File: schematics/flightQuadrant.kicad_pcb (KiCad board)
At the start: 2 copper layers, 50 x 62.5 mm, 15 parts, among them J1 Jack-DC, M1 M_ENG1, M2 M_ENG2, M3 M_BRK, M4 M_FLP, U1 L293D, U2 L293D

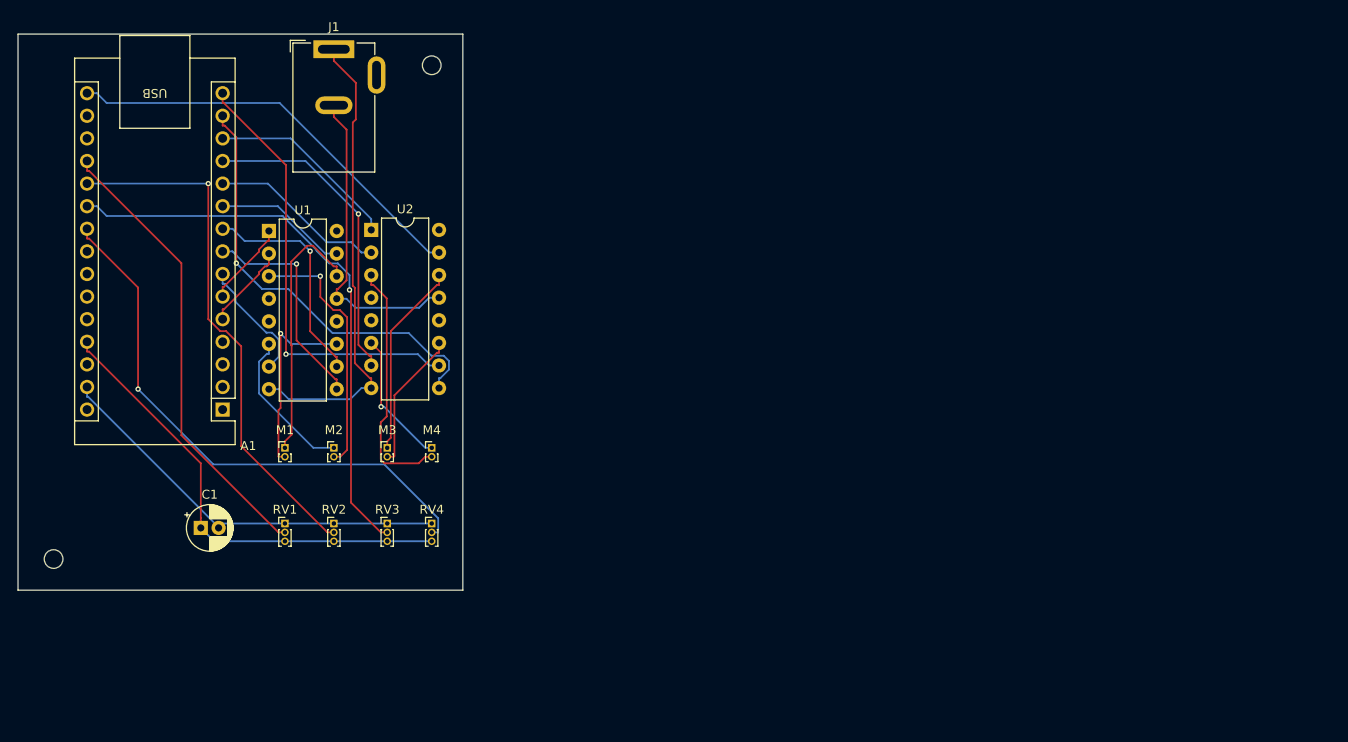
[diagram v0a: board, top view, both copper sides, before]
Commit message: Migrate to teeensyyyy 3.2
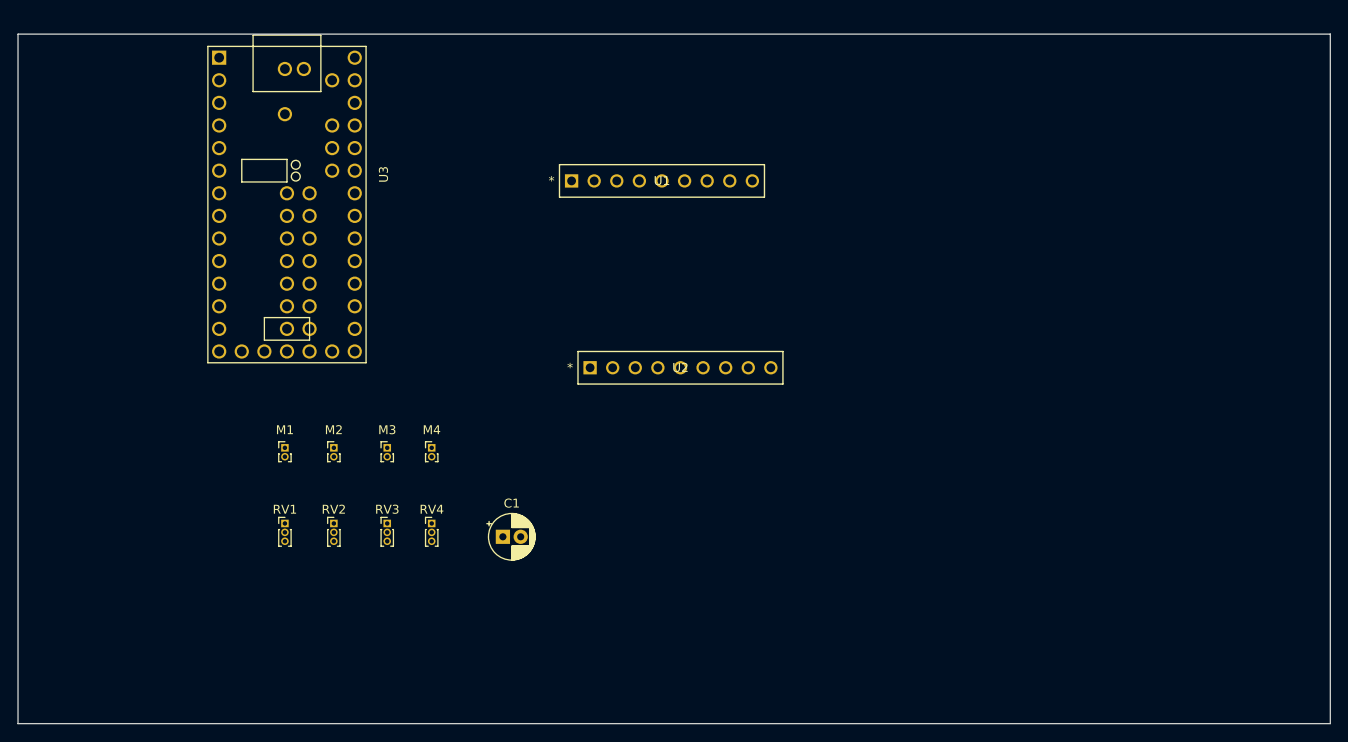
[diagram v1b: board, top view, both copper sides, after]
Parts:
- removed A1: Arduino_Nano_v3.x, Module:Arduino_Nano
- removed J1: Jack-DC, Connector_BarrelJack:BarrelJack_GCT_DCJ200-10-A_Horizontal
- removed REF**, p: MountingHole_2.1mm, MountingHole:MountingHole_2.1mm
- added U3: Teensy3.2, Teensy:Teensy30_31_32_All_Pins, F.Cu at (118.7, 63.2)
- U1, U2: value L293D -> ta7291sgo; footprint Package_DIP:DIP-16_W7.62mm -> TADriver:SIP9_TOS
- moved U1 34.5 mm to (150.7, 60.5)
- moved C1 34.0 mm to (143.0, 100.5)
- moved U2 29.1 mm to (152.8, 81.5)
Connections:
- M1 pad 1: Net-(U1-4Y) -> unconnected-(M1-Pad1)
- M1 pad 2: Net-(U1-3Y) -> unconnected-(M1-Pad2)
- M2 pad 1: Net-(U1-2Y) -> unconnected-(M2-Pad1)
- M2 pad 2: Net-(U1-1Y) -> unconnected-(M2-Pad2)
- M3 pad 1: Net-(U2-4Y) -> unconnected-(M3-Pad1)
- M3 pad 2: Net-(U2-3Y) -> unconnected-(M3-Pad2)
- M4 pad 1: Net-(U2-2Y) -> unconnected-(M4-Pad1)
- M4 pad 2: Net-(U2-1Y) -> unconnected-(M4-Pad2)
- RV1 pad 2: Net-(A1-A0) -> unconnected-(RV1-Pad2)
- RV2 pad 2: Net-(A1-A1) -> unconnected-(RV2-Pad2)
- RV3 pad 2: Net-(A1-A2) -> unconnected-(RV3-Pad2)
- RV4 pad 2: Net-(A1-A3) -> unconnected-(RV4-Pad2)
- U1 pad 1: Net-(A1-D3) -> unconnected-(U1-IN2-Pad1)
- U1 pad 2: Net-(A1-D2) -> unconnected-(U1-VCC-Pad2)
- U1 pad 3: Net-(U1-1Y) -> unconnected-(U1-OUT2-Pad3)
- U1 pad 6: Net-(U1-2Y) -> unconnected-(U1-VS-Pad6)
- U1 pad 7: Net-(A1-D4) -> unconnected-(U1-OUT1-Pad7)
- U1 pad 8: Net-(U1-VCC2) -> unconnected-(U1-VREF-Pad8)
- U1 pad 9: Net-(A1-D5) -> unconnected-(U1-IN1-Pad9)
- U2 pad 1: Net-(A1-D10) -> unconnected-(U2-IN2-Pad1)
- U2 pad 2: Net-(A1-D8) -> unconnected-(U2-VCC-Pad2)
- U2 pad 3: Net-(U2-1Y) -> unconnected-(U2-OUT2-Pad3)
- U2 pad 6: Net-(U2-2Y) -> unconnected-(U2-VS-Pad6)
- U2 pad 7: Net-(A1-D9) -> unconnected-(U2-OUT1-Pad7)
- U2 pad 8: Net-(U1-VCC2) -> unconnected-(U2-VREF-Pad8)
- U2 pad 9: Net-(A1-D11) -> unconnected-(U2-IN1-Pad9)
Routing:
- net Net-(A1-A2): track 63.9 -> 0.00 mm, vias 1 -> 0
- net Net-(A1-A3): track 62.6 -> 0.00 mm, vias 1 -> 0
- net Net-(A1-A1): track 59.5 -> 0.00 mm, vias 1 -> 0
- net Net-(C1-Pad1): track 52.9 -> 0.00 mm
- net Net-(U1-VCC2): track 52.7 -> 0.00 mm
- net Net-(A1-A0): track 51.5 -> 0.00 mm
- net Net-(A1-D12): track 50.1 -> 0.00 mm, vias 1 -> 0
- net Net-(A1-D11): track 49.4 -> 0.00 mm, vias 1 -> 0
- net Net-(A1-D13): track 47.0 -> 0.00 mm
- net Net-(C1-Pad2): track 46.2 -> 0.00 mm
- net Net-(A1-D9): track 35.5 -> 0.00 mm, vias 1 -> 0
- net Net-(J1-Pad2): track 35.3 -> 0.00 mm
- net Net-(U1-4Y): track 29.2 -> 0.00 mm
- net Net-(U1-1Y): track 28.8 -> 0.00 mm, vias 1 -> 0
- net Net-(U2-1Y): track 28.1 -> 0.00 mm
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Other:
- board size 50 x 62.5 mm -> 147.5 x 77.5 mm
